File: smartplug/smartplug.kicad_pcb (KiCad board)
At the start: 2 copper layers, 17 parts, among them J1 Conn_01x03_Male, J2 Conn_01x03_Female, K1 ALA2F12, U1 RAC01-05SGA, U2 ADP2302ARDZ-5.0-R7, U3 PHOTON, U4 NUD3112LT1G

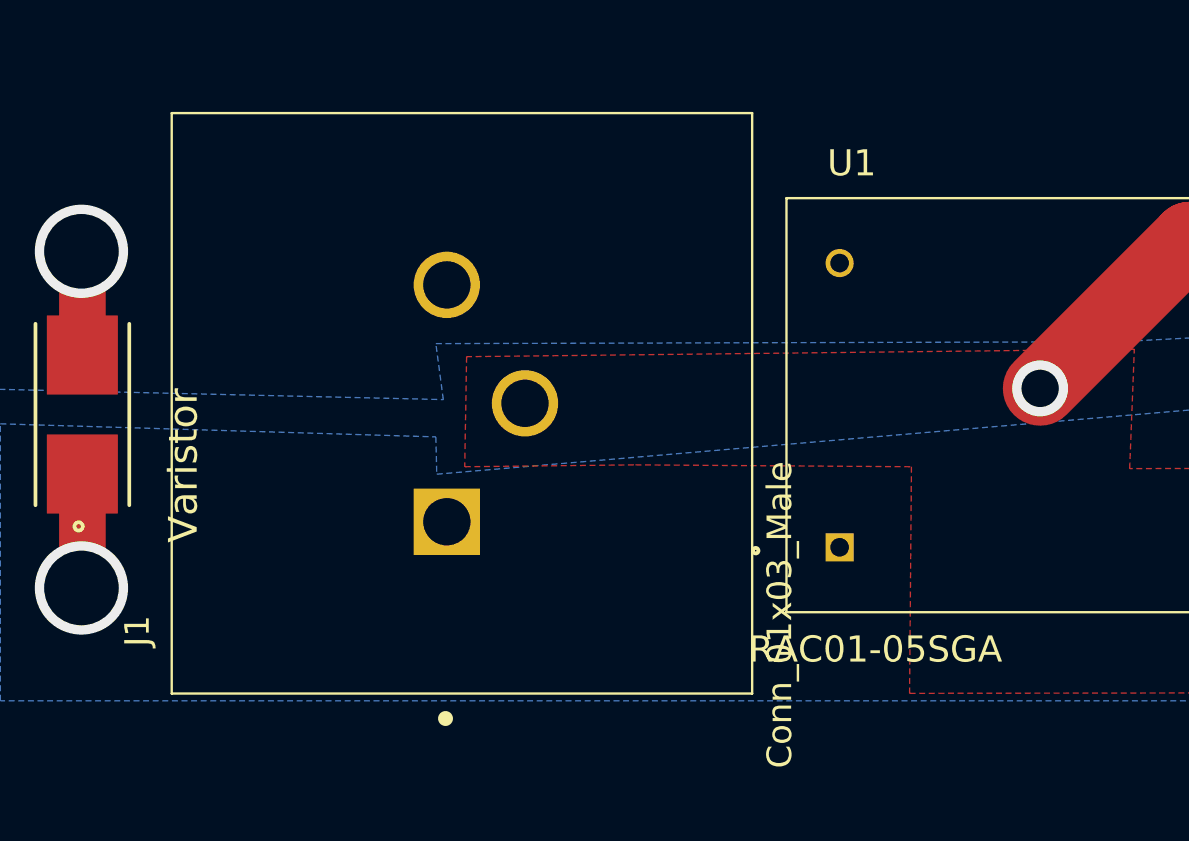
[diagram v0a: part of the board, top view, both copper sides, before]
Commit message: added connector footprint and updated PCB
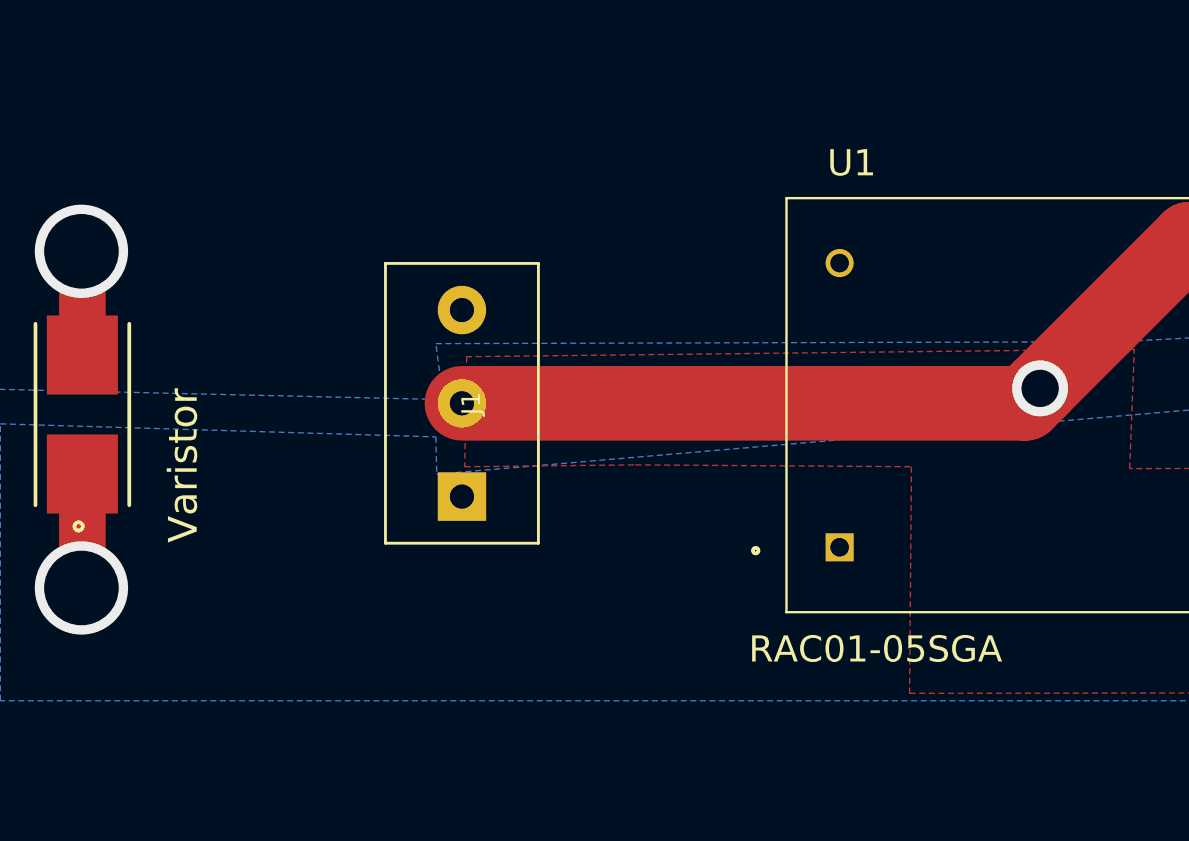
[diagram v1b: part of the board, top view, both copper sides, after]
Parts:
- J1: footprint female_plug_new:TE_3-213598-2-new -> term_block_3pos:1985852
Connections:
- U2 pad 6: (no net) -> Net-(U2-Pad6)
- U3 pad 10: (no net) -> Net-(U3-Pad10)
- U3 pad 11: (no net) -> Net-(U3-Pad11)
- U3 pad 12: (no net) -> Net-(U3-Pad12)
- U3 pad 13: (no net) -> Net-(U3-Pad13)
- U3 pad 14: (no net) -> Net-(U3-Pad14)
- U3 pad 15: (no net) -> Net-(U3-Pad15)
- U3 pad 16: (no net) -> Net-(U3-Pad16)
- U3 pad 17: (no net) -> Net-(U3-Pad17)
- U3 pad 18: (no net) -> Net-(U3-Pad18)
- U3 pad 19: (no net) -> Net-(U3-Pad19)
- U3 pad 22: (no net) -> Net-(U3-Pad22)
- U3 pad 23: (no net) -> Net-(U3-Pad23)
- U3 pad 24: (no net) -> Net-(U3-Pad24)
- U3 pad 3: (no net) -> Net-(U3-Pad3)
- U3 pad 4: (no net) -> Net-(U3-Pad4)
- U3 pad 5: (no net) -> Net-(U3-Pad5)
- U3 pad 6: (no net) -> Net-(U3-Pad6)
- U3 pad 7: (no net) -> Net-(U3-Pad7)
- U3 pad 8: (no net) -> Net-(U3-Pad8)
- U3 pad 9: (no net) -> Net-(U3-Pad9)
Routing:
- net GND: track 135.9 -> 167.3 mm
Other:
- net class Default: trace_width 0.3 -> 4

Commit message: Fixed clearances and added silkscreen
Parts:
- added G***: LOGO, logos:bac-logo, F.Cu at (105.0, 65.0)
- added G***: LOGO, logos:ieee-logo-inv, F.Cu at (122.0, 65.0)
- R1: footprint Resistor_SMD:R_0402_1005Metric -> Resistor_SMD:R_0805_2012Metric
- R2: value R -> 56
- U4: value NUD3112LT1G -> NUD3112
- moved J2 100.7 mm to (237.3, 93.3)
- moved U3 100.7 mm to (170.3, 109.8)
- moved C1 100.7 mm to (152.3, 95.0)
- moved C2 100.7 mm to (159.8, 95.3)
- moved C3 100.7 mm to (147.9, 87.8)
- moved C4 100.7 mm to (152.8, 87.9)
- moved D1 100.7 mm to (158.6, 90.3)
- moved D2 100.7 mm to (170.7, 71.7)
- moved K1 100.7 mm to (208.5, 93.6)
- moved L1 100.7 mm to (158.2, 78.2)
- moved R1 100.7 mm to (153.1, 102.6)
- moved R2 100.7 mm to (167.0, 72.5)
- moved U1 100.7 mm to (133.4, 101.8)
- moved U2 100.7 mm to (158.2, 100.6)
- moved U4 100.7 mm to (193.5, 93.0)
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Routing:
- net GND: track 167.3 -> 137.1 mm
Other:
- board outline added: 167 x 83 mm
- net class Default: clearance 0.5 -> 0.1; trace_width 4 -> 1
- rule trace_clearance: 0.5 -> 0.1
- board text added: "Jeremiah Marcum, Riley Lyman, Damon Anderson"

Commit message: pass DFM
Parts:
- J2: moved to B.Cu
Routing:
- net GND: track 137.1 -> 130.3 mm
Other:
- net class Default: trace_width 1 -> 2
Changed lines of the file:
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@@
-(kicad_pcb (version 20171130) (host pcbnew "(5.0.2)-1")
+(kicad_pcb (version 20171130) (host pcbnew 5.0.2-bee76a0~70~ubuntu18.04.1)
   (general
     (thickness 1.6)
@@
   )
   (setup
-    (last_trace_width 1)
+    (last_trace_width 2)
     (trace_clearance 0.1)
     (zone_clearance 2)
@@
       (outputformat 1)
       (mirror false)
-      (drillshape 1)
+      (drillshape 0)
       (scaleselection 1)
-      (outputdirectory ""))
+      (outputdirectory "DFM"))
   )
   (net 0 "")
@@
   (net_class Default "This is the default net class."
     (clearance 0.1)
-    (trace_width 1)
+    (trace_width 2)
     (via_dia 0.8)
     (via_drill 0.4)
@@
     )
   )
-  (module female_plug_new:TE_3-213598-2-new (layer F.Cu)
+  (module female_plug_new:TE_3-213598-2-new (layer B.Cu)
     (at 237.35 93.35 90)
-    (fp_text reference J2 (at -12.2056 -17.4005 90) (layer F.SilkS)
-      (effects (font (size 1.32005 1.32005) (thickness 0.05)))
-    )
-    (fp_text value Conn_01x03_Female (at -11.3413 17.0387 90) (layer F.SilkS)
-      (effects (font (size 1.32204 1.32204) (thickness 0.05)))
-    )
-    (fp_line (start -15.56 -15.56) (end -15.56 15.56) (layer F.SilkS) (width 0.127))
-    (fp_line (start -15.56 15.56) (end 15.56 15.56) (layer F.SilkS) (width 0.127))
-    (fp_line (start 15.56 15.56) (end 15.56 -15.56) (layer F.SilkS) (width 0.127))
-    (fp_line (start 15.56 -15.56) (end -15.56 -15.56) (layer F.SilkS) (width 0.127))
-    (fp_line (start -15.81 -15.81) (end -15.81 15.81) (layer Eco1.User) (width 0.05))
-    (fp_line (start -15.81 15.81) (end 15.81 15.81) (layer Eco1.User) (width 0.05))
-    (fp_line (start 15.81 15.81) (end 15.81 -15.81) (layer Eco1.User) (width 0.05))
-    (fp_line (start 15.81 -15.81) (end -15.81 -15.81) (layer Eco1.User) (width 0.05))
-    (fp_circle (center -16.9 -0.88) (end -16.7 -0.88) (layer F.SilkS) (width 0.4))
-    (fp_line (start -15.56 -15.56) (end -15.56 15.56) (layer Eco2.User) (width 0.127))
-    (fp_line (start -15.56 15.56) (end 15.56 15.56) (layer Eco2.User) (width 0.127))
-    (fp_line (start 15.56 15.56) (end 15.56 -15.56) (layer Eco2.User) (width 0.127))
-    (fp_line (start 15.56 -15.56) (end -15.56 -15.56) (layer Eco2.User) (width 0.127))
-    (pad 1 thru_hole rect (at -6.35 -0.81 90) (size 3.556 3.556) (drill 2.54) (layers *.Cu *.Mask)
+    (fp_text reference J2 (at -12.2056 17.4005 90) (layer B.SilkS)
+      (effects (font (size 1.32005 1.32005) (thickness 0.05)) (justify mirror))
+    )
+    (fp_text value Conn_01x03_Female (at -11.3413 -17.0387 90) (layer B.SilkS)
+      (effects (font (size 1.32204 1.32204) (thickness 0.05)) (justify mirror))
+    )
+    (fp_line (start -15.56 15.56) (end -15.56 -15.56) (layer B.SilkS) (width 0.127))
+    (fp_line (start -15.56 -15.56) (end 15.56 -15.56) (layer B.SilkS) (width 0.127))
+    (fp_line (start 15.56 -15.56) (end 15.56 15.56) (layer B.SilkS) (width 0.127))
+    (fp_line (start 15.56 15.56) (end -15.56 15.56) (layer B.SilkS) (width 0.127))
+    (fp_line (start -15.81 15.81) (end -15.81 -15.81) (layer Eco1.User) (width 0.05))
+    (fp_line (start -15.81 -15.81) (end 15.81 -15.81) (layer Eco1.User) (width 0.05))
+    (fp_line (start 15.81 -15.81) (end 15.81 15.81) (layer Eco1.User) (width 0.05))
+    (fp_line (start 15.81 15.81) (end -15.81 15.81) (layer Eco1.User) (width 0.05))
+    (fp_circle (center -16.9 0.88) (end -16.7 0.88) (layer B.SilkS) (width 0.4))
+    (fp_line (start -15.56 15.56) (end -15.56 -15.56) (layer Eco2.User) (width 0.127))
+    (fp_line (start -15.56 -15.56) (end 15.56 -15.56) (layer Eco2.User) (width 0.127))
+    (fp_line (start 15.56 -15.56) (end 15.56 15.56) (layer Eco2.User) (width 0.127))
+    (fp_line (start 15.56 15.56) (end -15.56 15.56) (layer Eco2.User) (width 0.127))
+    (pad 1 thru_hole rect (at -6.35 0.81 90) (size 3.556 3.556) (drill 2.54) (layers *.Cu *.Mask)
       (net 10 "Net-(J2-Pad1)"))
-    (pad 3 thru_hole circle (at 6.35 -0.81 90) (size 3.556 3.556) (drill 2.54) (layers *.Cu *.Mask)
+    (pad 3 thru_hole circle (at 6.35 0.81 90) (size 3.556 3.556) (drill 2.54) (layers *.Cu *.Mask)
       (net 11 "Net-(J2-Pad3)"))
-    (pad 2 thru_hole circle (at 0 3.38 90) (size 3.556 3.556) (drill 2.54) (layers *.Cu *.Mask)
+    (pad 2 thru_hole circle (at 0 -3.38 90) (size 3.556 3.556) (drill 2.54) (layers *.Cu *.Mask)
       (net 1 GND))
   )
@@
   (segment (start 192.2554 93.8898) (end 192.2554 113.3054) (width 2) (layer F.Cu) (net 1))
   (segment (start 212.5 93.35) (end 192.4 113.45) (width 2) (layer F.Cu) (net 1))
-  (segment (start 240.73 93.35) (end 212.5 93.35) (width 2) (layer F.Cu) (net 1))
   (segment (start 167.556237 73.943737) (end 167 73.3875) (width 0.3) (layer F.Cu) (net 1))
   (segment (start 171.939801 78.327301) (end 167.556237 73.943737) (width 0.3) (layer F.Cu) (net 1))
@@
   (segment (start 170.35 84.45) (end 171.289799 83.510201) (width 0.3) (layer F.Cu) (net 1))
   (segment (start 129.35 101.65) (end 130.15 100.85) (width 4) (layer F.Cu) (net 1))
+  (segment (start 212.5 93.35) (end 233.97 93.35) (width 2) (layer F.Cu) (net 1))
   (via (at 141.45 99.2) (size 4) (drill 3) (layers F.Cu B.Cu) (net 2))
   (segment (start 198.25 88.197094) (end 198.25 88.664607) (width 2.3) (layer B.Cu) (net 2))
@@
     (polygon
       (pts
-        (xy 87.975 98.1625) (xy 97.35 98.0375) (xy 98.3 98) (xy 110.398856 98.083814) (xy 155.4 73.4)
+        (xy 87.975 98.1625) (xy 97.35 98.0375) (xy 98.3 98) (xy 112.881428 98.955907) (xy 157.882572 74.272093)
         (xy 167.1 73.4) (xy 183.3 73.5) (xy 195.7 73.7) (xy 205.3 91) (xy 214.8 91.2)
         (xy 215.4 54.05) (xy 88.025 53.95)

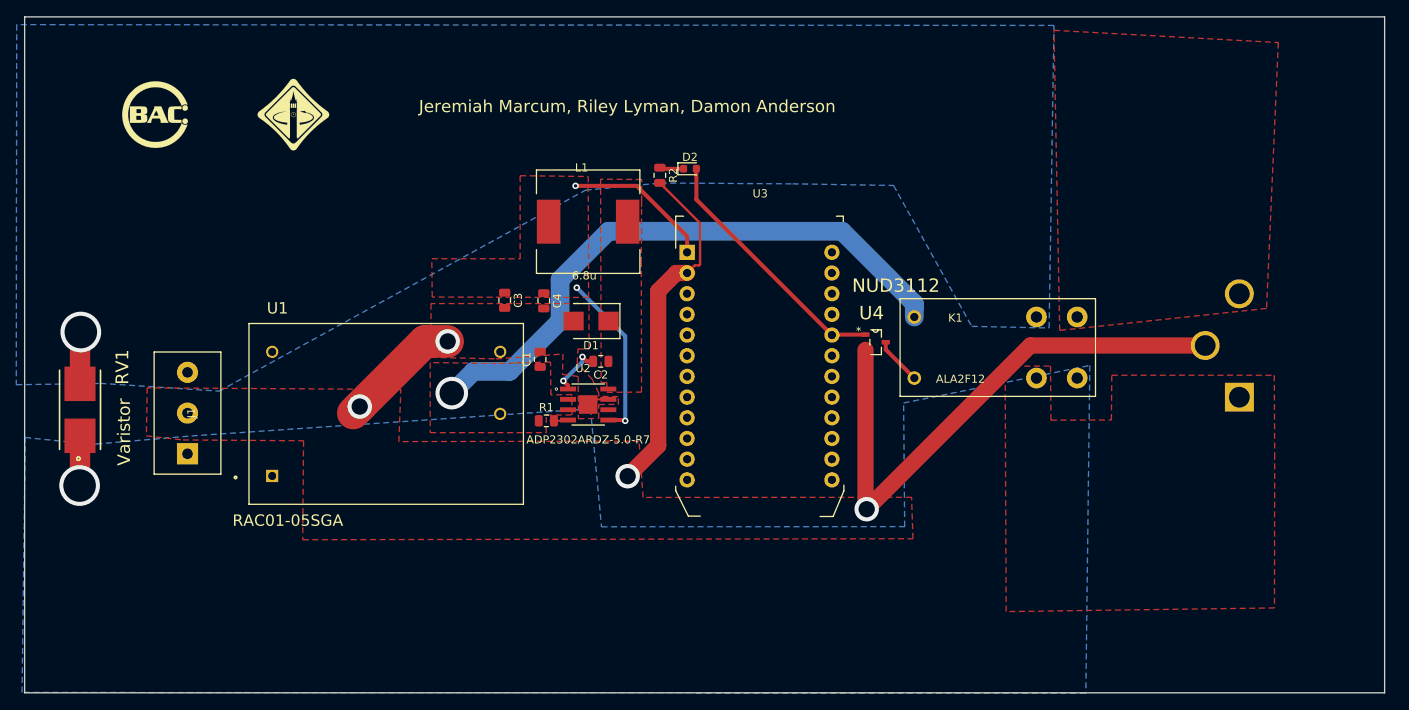
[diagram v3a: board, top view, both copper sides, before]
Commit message: rearranged board to reduce area
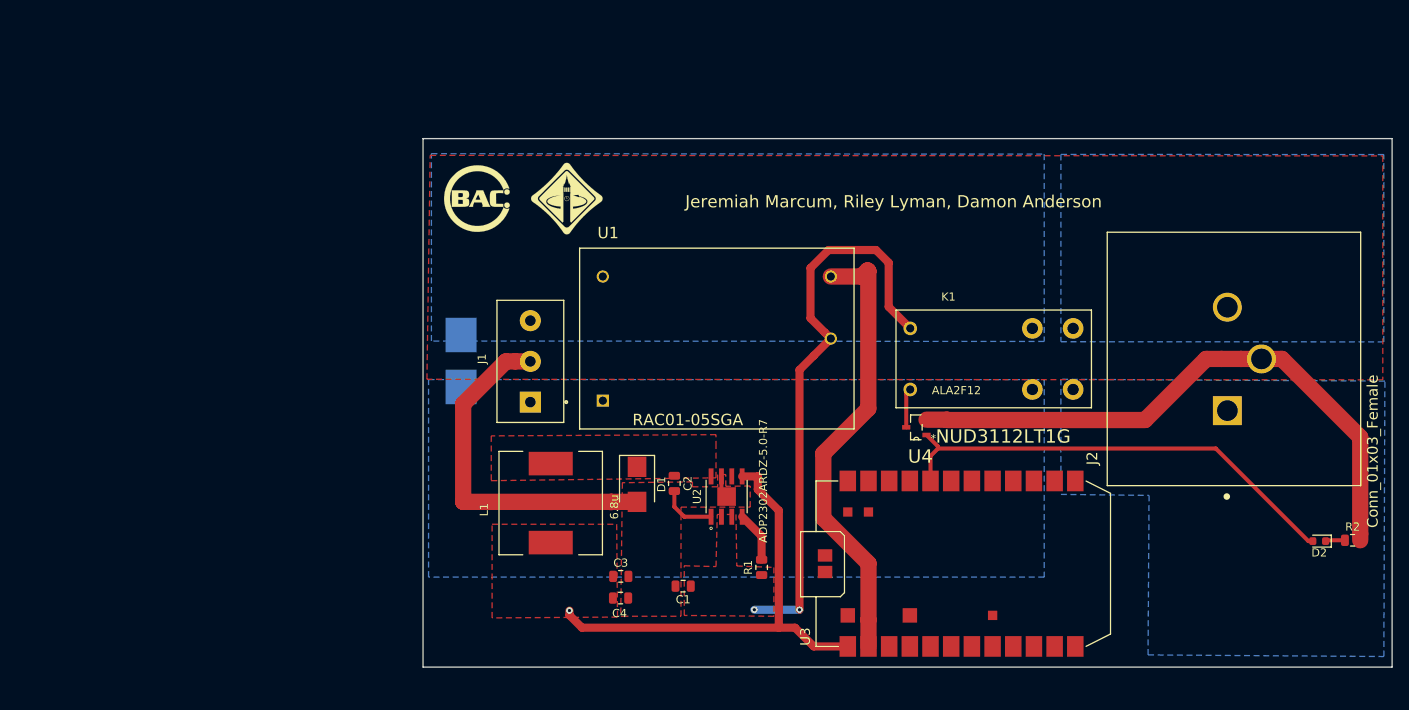
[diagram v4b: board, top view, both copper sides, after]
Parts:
- J2: moved to F.Cu
- RV1: moved to B.Cu
- U3: footprint digikey-footprints:Particle_Photon -> particle:photon_smd
- U4: value NUD3112 -> NUD3112LT1G
- moved R2 96.2 mm to (252.1, 117.3), turned to 0 degrees
- moved D2 89.8 mm to (248.0, 117.4), turned to 180 degrees
- moved RV1 47.2 mm to (142.6, 95.2)
- moved J1 42.6 mm to (151.1, 95.3)
- moved U1 41.6 mm to (174.0, 92.5)
- moved G*** 40.8 mm to (144.5, 75.3)
- moved C4 37.7 mm to (162.2, 124.4), turned to 0 degrees
- moved C3 36.8 mm to (162.2, 121.7), turned to 0 degrees
- moved G*** 35.1 mm to (155.6, 75.3)
- moved L1 34.9 mm to (153.6, 112.7), turned to 90 degrees
- moved C1 32.9 mm to (169.9, 122.9), turned to 180 degrees
- moved R1 32.0 mm to (179.5, 120.6), turned to 90 degrees
- moved U3 25.9 mm to (186.2, 130.3), turned to 90 degrees
- moved D1 20.8 mm to (164.2, 110.4), turned to 270 degrees
- moved U2 20.4 mm to (175.2, 111.9), turned to 90 degrees
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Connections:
- net Net-(J2-Pad3) renamed /out_VAC-
- J2 pad 1: Net-(J2-Pad1) -> /out_VAC+
- K1 pad 3: /VAC+ -> /out_VAC+
- K1 pad 4: Net-(J2-Pad1) -> /VAC+
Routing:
- net GND: track 130.3 -> 176.4 mm, vias 4 -> 0
- net Net-(D2-Pad2): track 31.5 -> 57.3 mm
- net /5VDC: track 39.2 -> 57.9 mm, vias 3 -> 1
- net /VAC+: track 6.13 -> 0.00 mm, vias 1 -> 0
- net /VAC-: track 5.58 -> 0.00 mm, vias 1 -> 0
- net Net-(R1-Pad2): track 2.21 -> 6.28 mm
- net /12VDC: track 73.3 -> 70.5 mm, vias 1 -> 2
- net Net-(K1-Pad1): track 5.85 -> 4.85 mm
- net Net-(C2-Pad2): track 6.70 -> 7.64 mm, vias 2 -> 0
- net Net-(D2-Pad1): track 2.97 -> 2.42 mm
- added copper zone on B.Cu, net /out_VAC+
- added copper zone on B.Cu, net /out_VAC-
- removed copper zone on F.Cu, net /out_VAC-
- removed copper zone on F.Cu, net Net-(J2-Pad1)
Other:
- board size 167 x 83 mm -> 119 x 64.9 mm
- net class Default: clearance 0.1 -> 0.16
- rule trace_clearance: 0.1 -> 0.16
